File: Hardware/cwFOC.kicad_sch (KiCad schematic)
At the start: 6 parts

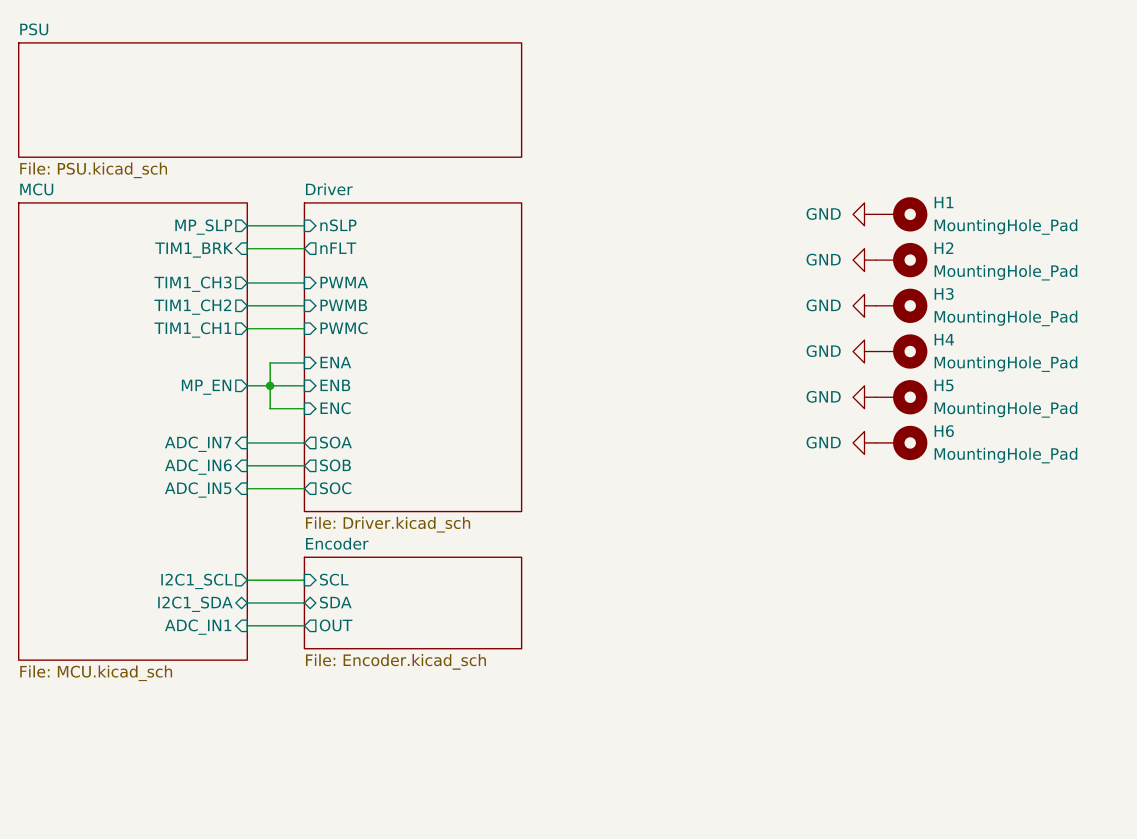
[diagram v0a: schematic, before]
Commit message: 完成原理图设计，完成初步布局布线
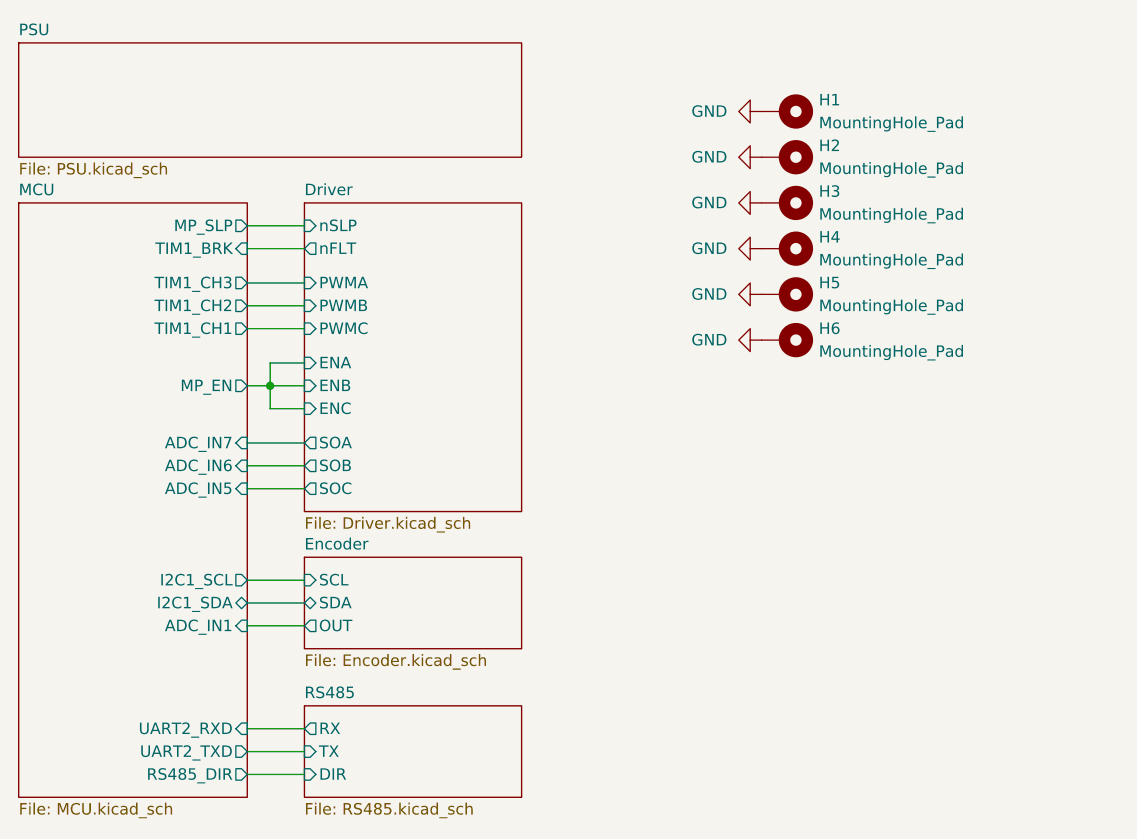
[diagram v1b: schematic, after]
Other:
- added sheet RS485 (RS485.kicad_sch)
- sheet MCU ports: added RS485_DIR, UART2_RXD, UART2_TXD; removed none
- moved on the sheet: H1, H2, H3, H4, H5, H6

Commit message: 完善原理图设计、添加硬件README
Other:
- sheet MCU ports: added ADC_IN3, ADC_IN4, UART3_RXD, UART3_TXD; removed ADC_IN6, ADC_IN7, UART2_RXD, UART2_TXD
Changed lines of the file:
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@@
-      (effects (font (size 1.27 1.27)) (justify right))
-    )
-    (pin "ADC_IN7" input (at 139.7 111.76 0)
-      (effects (font (size 1.27 1.27)) (justify right))
-    )
-    (pin "ADC_IN5" input (at 139.7 116.84 0)
-      (effects (font (size 1.27 1.27)) (justify right))
-    )
-    (pin "ADC_IN6" input (at 139.7 114.3 0)
       (effects (font (size 1.27 1.27)) (justify right))
     )
@@
       (effects (font (size 1.27 1.27)) (justify right))
     )
-    (pin "UART2_TXD" output (at 139.7 146.05 0)
+    (pin "ADC_IN3" input (at 139.7 116.84 0)
       (effects (font (size 1.27 1.27)) (justify right))
     )
-    (pin "UART2_RXD" input (at 139.7 143.51 0)
+    (pin "ADC_IN4" input (at 139.7 114.3 0)
       (effects (font (size 1.27 1.27)) (justify right))
     )
+    (pin "ADC_IN5" input (at 139.7 111.76 0)
+      (effects (font (size 1.27 1.27)) (justify right))
+    )
+    (pin "UART3_TXD" output (at 139.7 146.05 0)
+      (effects (font (size 1.27 1.27)) (justify right))
+    )
+    (pin "UART3_RXD" input (at 139.7 143.51 0)
+      (effects (font (size 1.27 1.27)) (justify right))
+    )

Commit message: 基本完成PCB设计
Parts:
- H1, H2, H3, H4, H5, H6: footprint MountingHole:MountingHole_2.2mm_M2_Pad_TopBottom -> myLib:MountingHole_2.2mm_M2
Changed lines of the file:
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@@
       (effects (font (size 1.27 1.27)) (justify left))
     )
-    (property "Footprint" "MountingHole:MountingHole_2.2mm_M2_Pad_TopBottom" (at 199.39 74.93 0)
+    (property "Footprint" "myLib:MountingHole_2.2mm_M2" (at 199.39 74.93 0)
       (effects (font (size 1.27 1.27)) hide)
     )
@@
       (effects (font (size 1.27 1.27)) (justify left))
     )
-    (property "Footprint" "MountingHole:MountingHole_2.2mm_M2_Pad_TopBottom" (at 199.39 85.09 0)
+    (property "Footprint" "myLib:MountingHole_2.2mm_M2" (at 199.39 85.09 0)
       (effects (font (size 1.27 1.27)) hide)
     )
@@
       (effects (font (size 1.27 1.27)) (justify left))
     )
-    (property "Footprint" "MountingHole:MountingHole_2.2mm_M2_Pad_TopBottom" (at 199.39 80.01 0)
+    (property "Footprint" "myLib:MountingHole_2.2mm_M2" (at 199.39 80.01 0)
       (effects (font (size 1.27 1.27)) hide)
     )
@@
       (effects (font (size 1.27 1.27)) (justify left))
     )
-    (property "Footprint" "MountingHole:MountingHole_2.2mm_M2_Pad_TopBottom" (at 199.39 100.33 0)
+    (property "Footprint" "myLib:MountingHole_2.2mm_M2" (at 199.39 100.33 0)
       (effects (font (size 1.27 1.27)) hide)
     )
@@
       (effects (font (size 1.27 1.27)) (justify left))
     )
-    (property "Footprint" "MountingHole:MountingHole_2.2mm_M2_Pad_TopBottom" (at 199.39 95.25 0)
+    (property "Footprint" "myLib:MountingHole_2.2mm_M2" (at 199.39 95.25 0)
       (effects (font (size 1.27 1.27)) hide)
     )
@@
       (effects (font (size 1.27 1.27)) (justify left))
     )
-    (property "Footprint" "MountingHole:MountingHole_2.2mm_M2_Pad_TopBottom" (at 199.39 90.17 0)
-      (effects (font (size 1.27 1.27)) hide)
-    )
+    (property "Footprint" "myLib:MountingHole_2.2mm_M2" (at 199.39 90.17 0)
+      (effects (font (size 1.27 1.27)) hide)
+    )

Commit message: 第一版硬件做好啦！(●'◡'●)
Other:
- company: akako -> Akako Industry
- title: mmFOC -> cwFOC
- moved on the sheet: H1, H2, H3, H4, H5, H6

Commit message: 小修小补，拉了点线
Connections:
- no-connect marks 0 -> 1
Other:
- sheet MCU ports: added none; removed ADC_IN1
- company: Akako Industry -> Akako Science & Industry
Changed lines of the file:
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@@
     (date "2023-03-19")
     (rev "1.0")
-    (company "Akako Industry")
+    (company "Akako Science & Industry")
     (comment 1 "赤紫绮")
     (comment 2 "赤紫绮")
@@
   (junction (at 142.24 105.41) (diameter 0) (color 0 0 0 0)
   )
+  (no_connect (at 146.05 132.08))
   (wire (pts (xy 139.7 87.63) (xy 146.05 87.63))
     (stroke (width 0) (type default))
@@
   )
   (wire (pts (xy 139.7 143.51) (xy 146.05 143.51))
-    (stroke (width 0) (type default))
-  )
-  (wire (pts (xy 139.7 132.08) (xy 146.05 132.08))
     (stroke (width 0) (type default))
   )
@@
       (effects (font (size 1.27 1.27)) (justify right))
     )
-    (pin "ADC_IN1" input (at 139.7 132.08 0)
-      (effects (font (size 1.27 1.27)) (justify right))
-    )

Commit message: 完成第二版硬件
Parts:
- removed H1, H2, H3, H4, H5, H6: MountingHole_Pad, myLib:MountingHole_2.2mm_M2, symbol Mechanical:MountingHole_Pad
- added H1, H2, H3, H4, H5, H6: MountingHole, myLib:MountingHole_2.2mm_M2, symbol Mechanical:MountingHole
